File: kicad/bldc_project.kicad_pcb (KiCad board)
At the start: 4 copper layers, 105 x 60 mm, 156 parts, among them J1 Conn_ARM_SWD_TagConnect_TC203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, J2 Screw_Terminal_01x03, J3 Screw_Terminal_01x03, J4 TYPE-C-31-M-12, Q1 IRFZ44N, Q2 IRFZ44N, Q3 IRFZ44N, Q4 IRFZ44N, Q5 IRFZ44N, Q6 IRFZ44N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

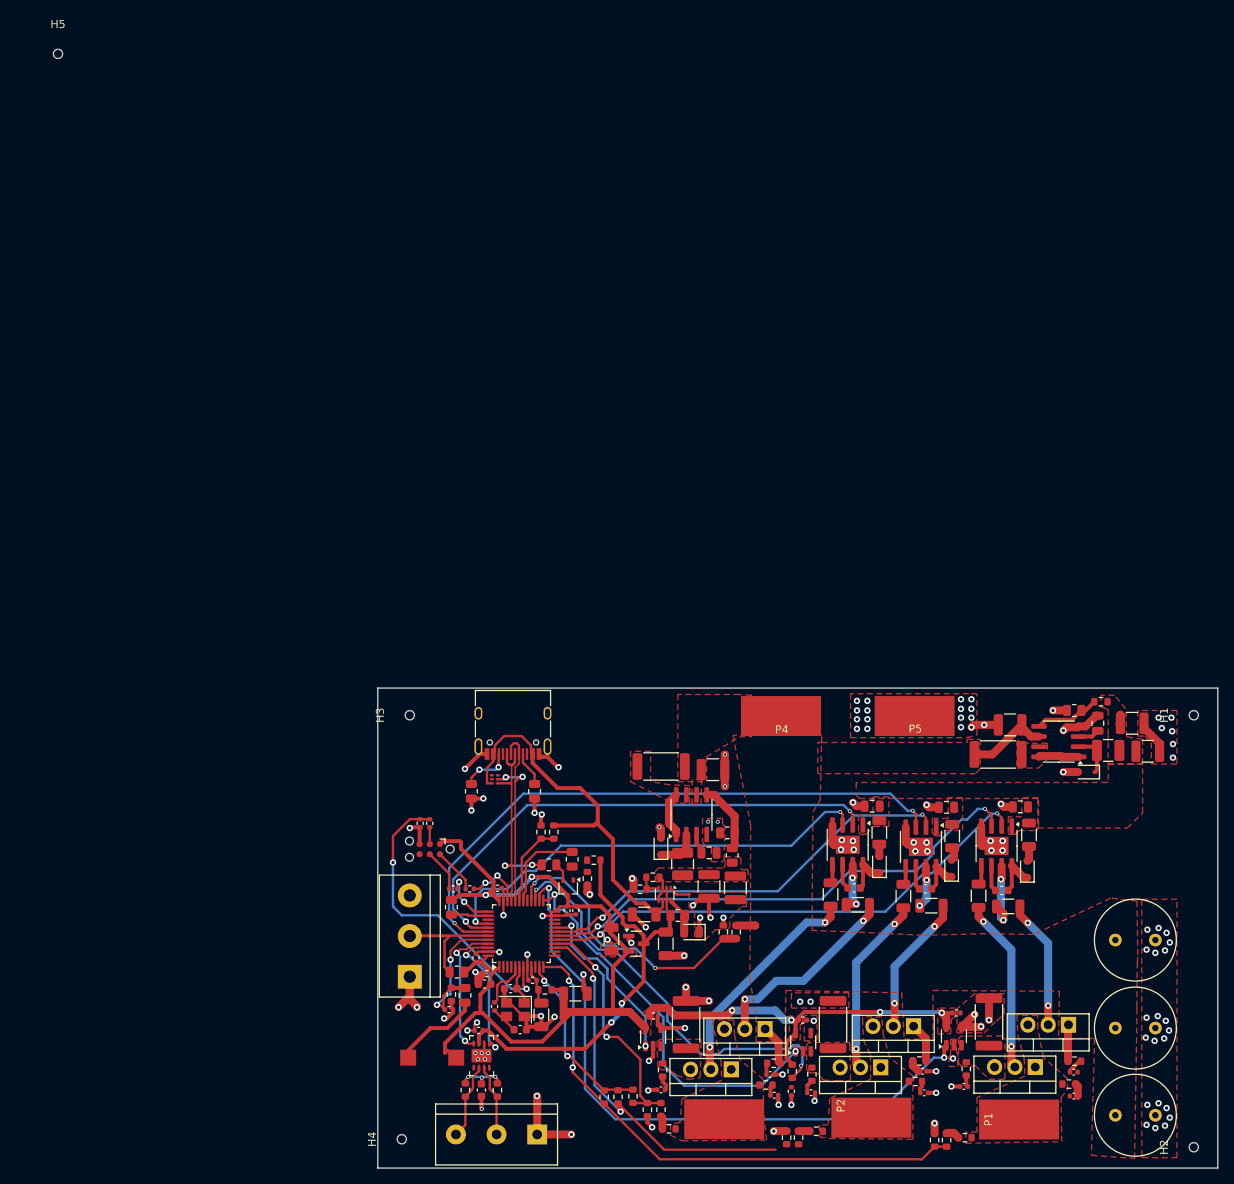
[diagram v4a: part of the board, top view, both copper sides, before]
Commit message: [kicad] Routing ERC completed, Minor footprint issues
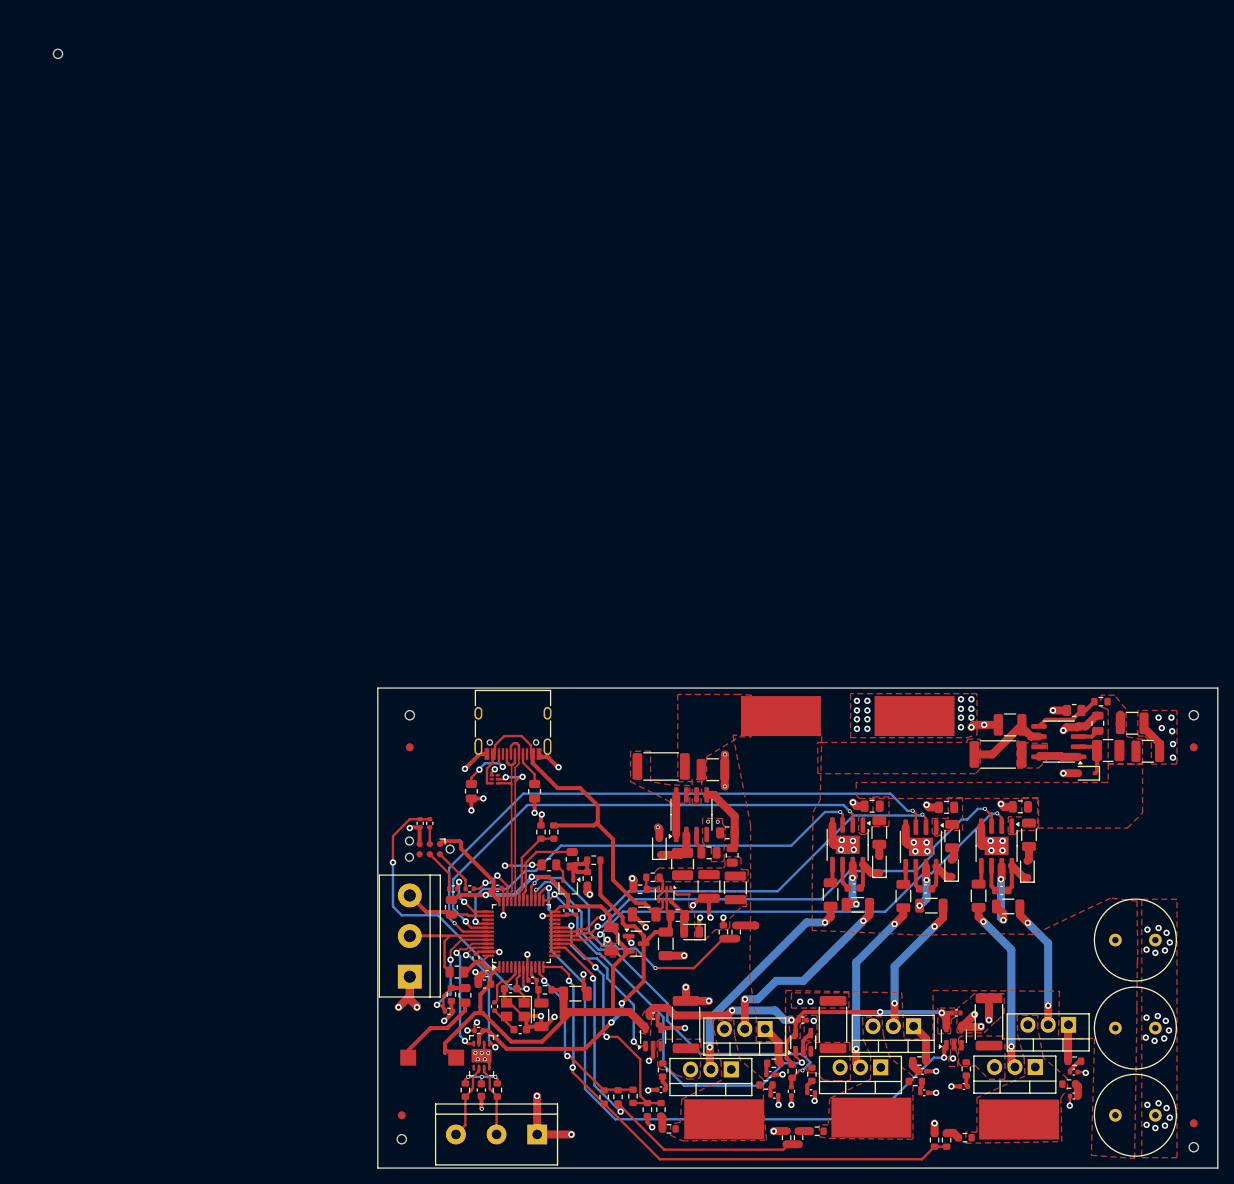
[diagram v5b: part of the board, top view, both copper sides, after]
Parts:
- added FM1: Fiducial, Fiducial:Fiducial_1mm_Mask2mm, F.Cu at (45.2, 87.9)
- added FM2: Fiducial, Fiducial:Fiducial_1mm_Mask2mm, F.Cu at (44.2, 133.9)
- added FM3: Fiducial, Fiducial:Fiducial_1mm_Mask2mm, F.Cu at (143.2, 134.9)
- added FM4: Fiducial, Fiducial:Fiducial_1mm_Mask2mm, F.Cu at (143.2, 87.9)
- moved C25 0.20 mm to (50.1, 120.9)
- moved D7 0.20 mm to (76.4, 100.3)
- moved D8 0.15 mm to (129.8, 91.2)
- moved R25 0.10 mm to (96.1, 135.9)
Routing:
- net GND: track 166.0 -> 173.7 mm, vias 127 -> 130
- net Net-(Q7-B): track 0.00 -> 7.62 mm
- net /CPU/I2C_SCL: track 4.64 -> 10.8 mm
- net PhaseV_DIV: track 48.5 -> 51.6 mm
- net PhaseV_CURRENT: track 48.9 -> 50.2 mm
- net Net-(J4-CC2): track 6.40 -> 7.51 mm
- net /CPU/MEAS_TEMP: track 51.5 -> 52.5 mm
- net /POWER/VBUCK5_IN: track 5.70 -> 4.95 mm
- net PhaseW_CURRENT: track 22.0 -> 22.6 mm

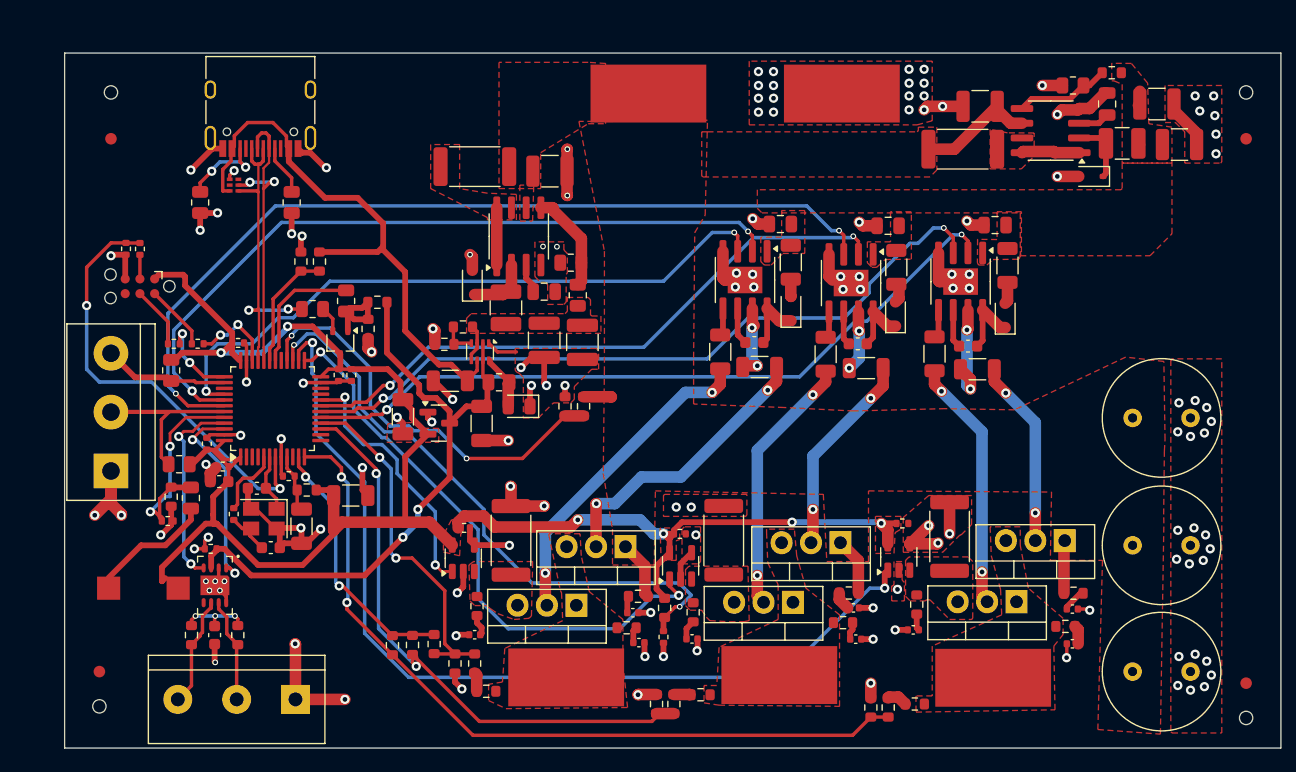
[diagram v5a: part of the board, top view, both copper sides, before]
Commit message: [kicad] Added silkscreen indicators for capacitors + screw terminal indications
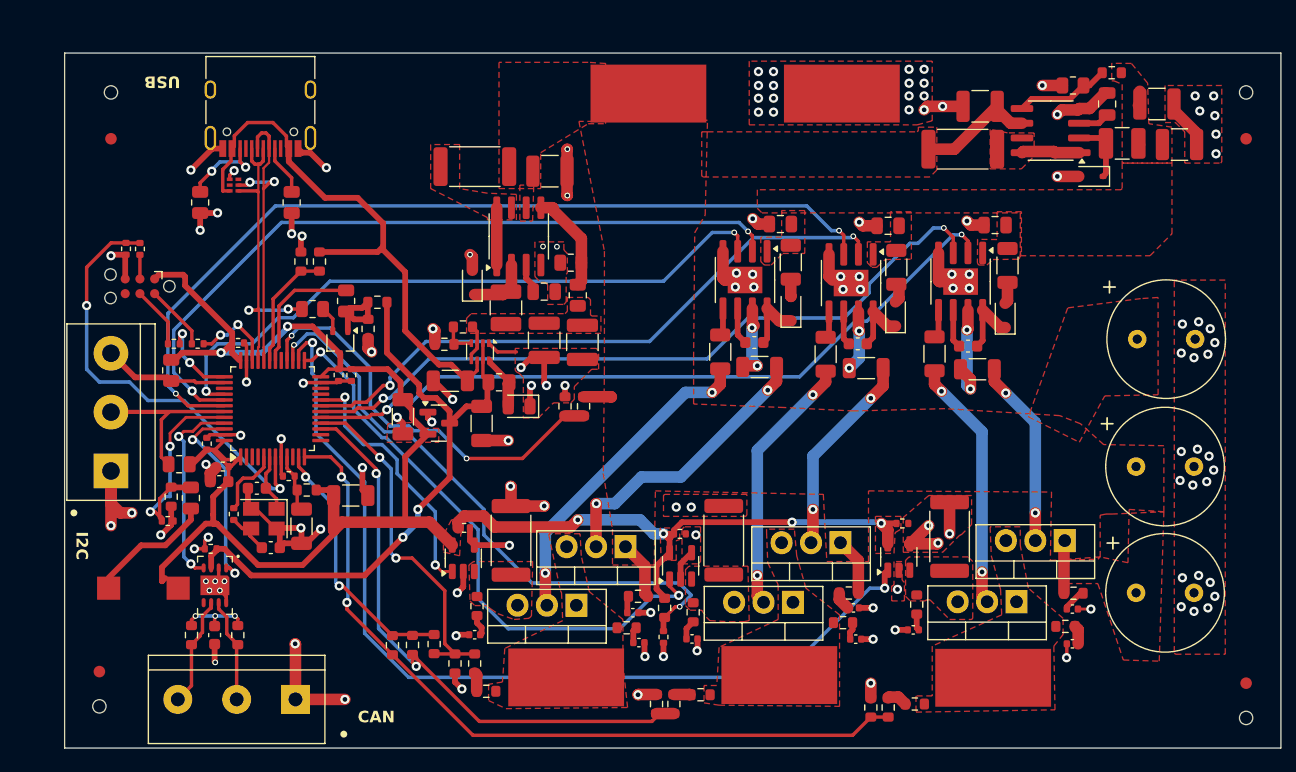
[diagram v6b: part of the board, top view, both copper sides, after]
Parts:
- moved C16 6.81 mm to (133.8, 105.2)
- moved C18 6.81 mm to (133.7, 127.1)
- moved C17 6.81 mm to (133.7, 116.2)
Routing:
- net GND: track 173.7 -> 174.8 mm
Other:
- board text added: "CAN"
- board text added: "I2C"
- board text added: "USB"
